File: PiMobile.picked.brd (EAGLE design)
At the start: 125 x 125 mm, 30 parts, among them IC1_0_BRAIN 78XX-VOLTAGE_REGULATORT, U1_0_BRAIN RASPBERRY-PI, U1_10_PENHOLDER PENHOLDER, U1_5_CASTER CASTERADAFRUIT-3/4IN

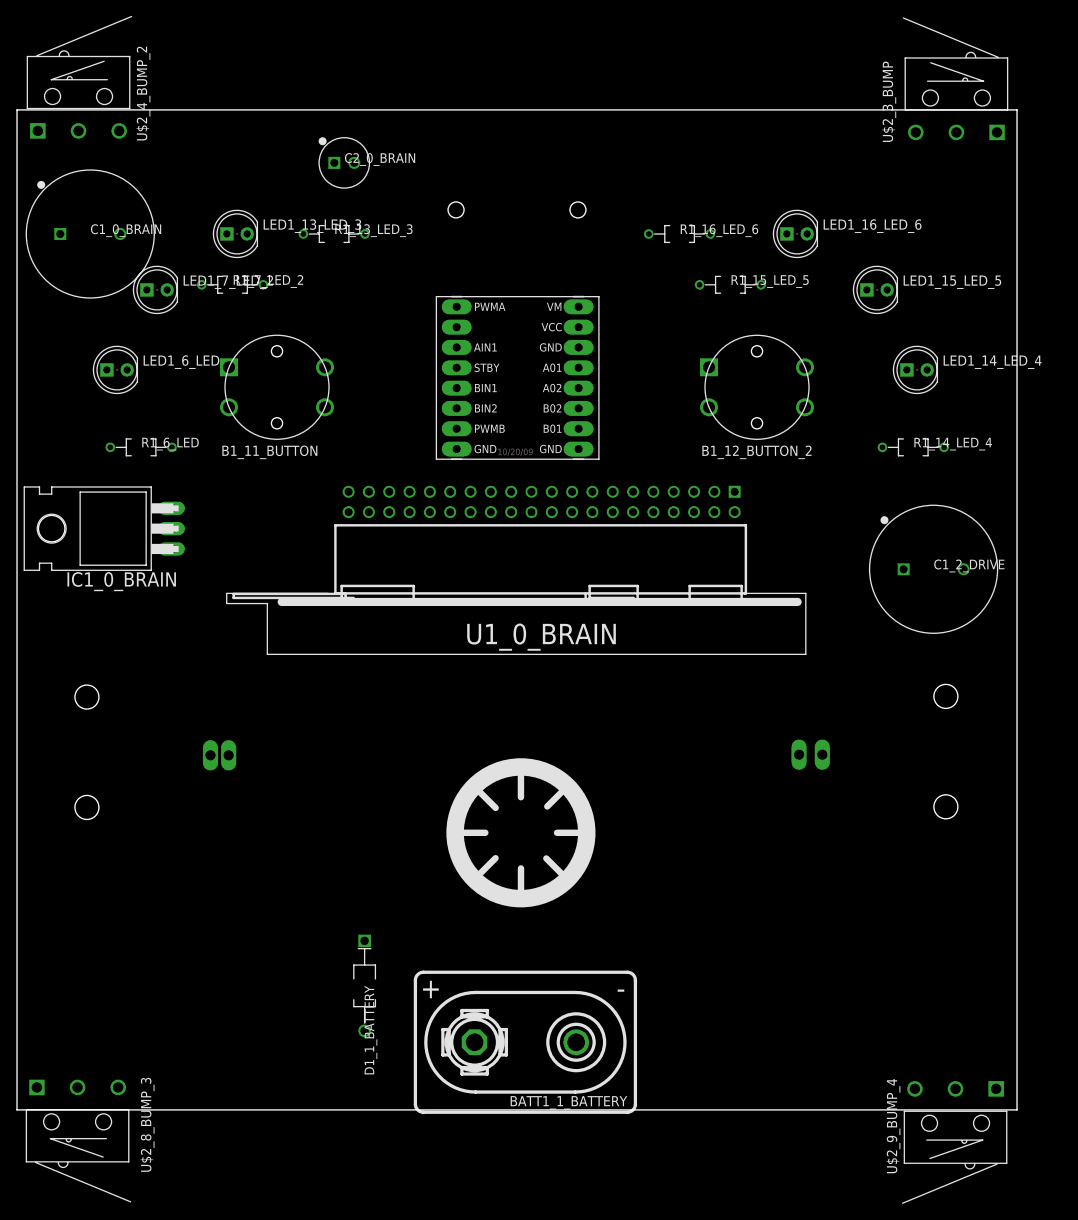
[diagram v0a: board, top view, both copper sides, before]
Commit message: got rid of cut out.  Ordered boards
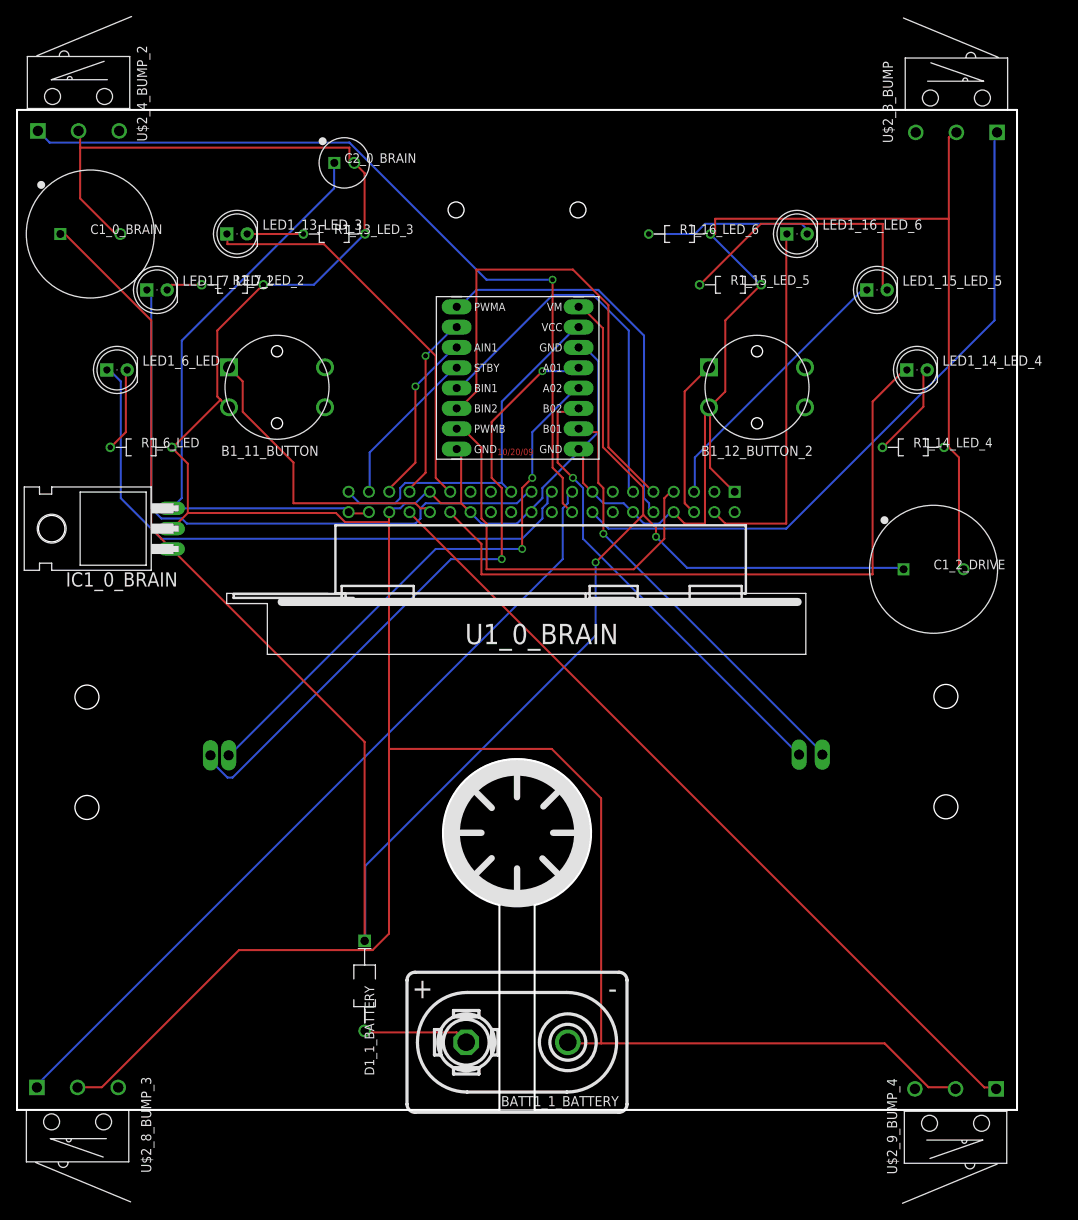
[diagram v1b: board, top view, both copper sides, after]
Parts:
- moved BATT1_1_BATTERY 1.05 mm to (0.00, -54.0)
- moved U1_10_PENHOLDER 0.49 mm to (0.00, -27.9)
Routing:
- net GND_0_BRAIN: track 0.00 -> 570.2 mm
- net POS_1_BATTERY: track 0.00 -> 237.8 mm, vias 0 -> 2
- net TXD0/GPIO14_0_BRAIN: track 0.00 -> 103.2 mm
- net GPIO11/SCLK_0_BRAIN: track 0.00 -> 102.3 mm
- net !CE0!/GPIO8_0_BRAIN: track 0.00 -> 102.1 mm, vias 0 -> 1
- net GPIO18_0_BRAIN: track 0.00 -> 85.8 mm
- net !CE!/GPIO7_0_BRAIN: track 0.00 -> 85.7 mm
- net A01_2_DRIVE: track 0.00 -> 81.2 mm, vias 0 -> 2
- net GPIO10/MOSI_0_BRAIN: track 0.00 -> 78.2 mm
- net GPIO9/MISO_0_BRAIN: track 0.00 -> 76.8 mm
- net 5V_0_BRAIN: track 0.00 -> 76.6 mm
- net A02_2_DRIVE: track 0.00 -> 70.7 mm, vias 0 -> 2
- net GPIO6_0_BRAIN: track 0.00 -> 62.6 mm
- net B02_2_DRIVE: track 0.00 -> 58.3 mm, vias 0 -> 1
- net B01_2_DRIVE: track 0.00 -> 54.5 mm, vias 0 -> 1
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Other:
- outline, holes or cut-outs redrawn
